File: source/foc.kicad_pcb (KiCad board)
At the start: 2 copper layers, 66.4 x 76.3 mm, 209 parts, among them J1001 Conn_01x04_Male, J1003 TYPE-C-31-M-12, P1 HALL_ENC, P2 SERVO, P3 SWD, P5 PH_A, P6 GND, P7 SUPPLY, P8 PH_B, P9 PH_C, Q1 FMMT593TA, Q10 CSD19536KCS, Q11 CSD19536KCS, Q12 CSD19536KCS, Q13 FMMT593TA, Q14 FMMT593TA, Q15 CSD19536KCS, Q16 CSD19536KCS, Q17 CSD19536KCS, Q18 CSD19536KCS, Q2 FMMT593TA, Q3 NCEP60T20, Q4 CSD19536KCS, Q5 CSD19536KCS, Q6 CSD19536KCS, Q7 FMMT593TA, Q8 FMMT593TA, Q9 CSD19536KCS, U10 TP2604-SR, U1002 TJA1050T/CM,118, U1003 HT7550, U1005 LM1117-3.3, U11 STM32F405RGT6, U2001 BMI160, U4 IRS21867S, U5 IRS21867S, U7 IRS21867S, U8 TX4130L/PW2902, U9 TP2604-SR, Y1001 Crystal_GND24

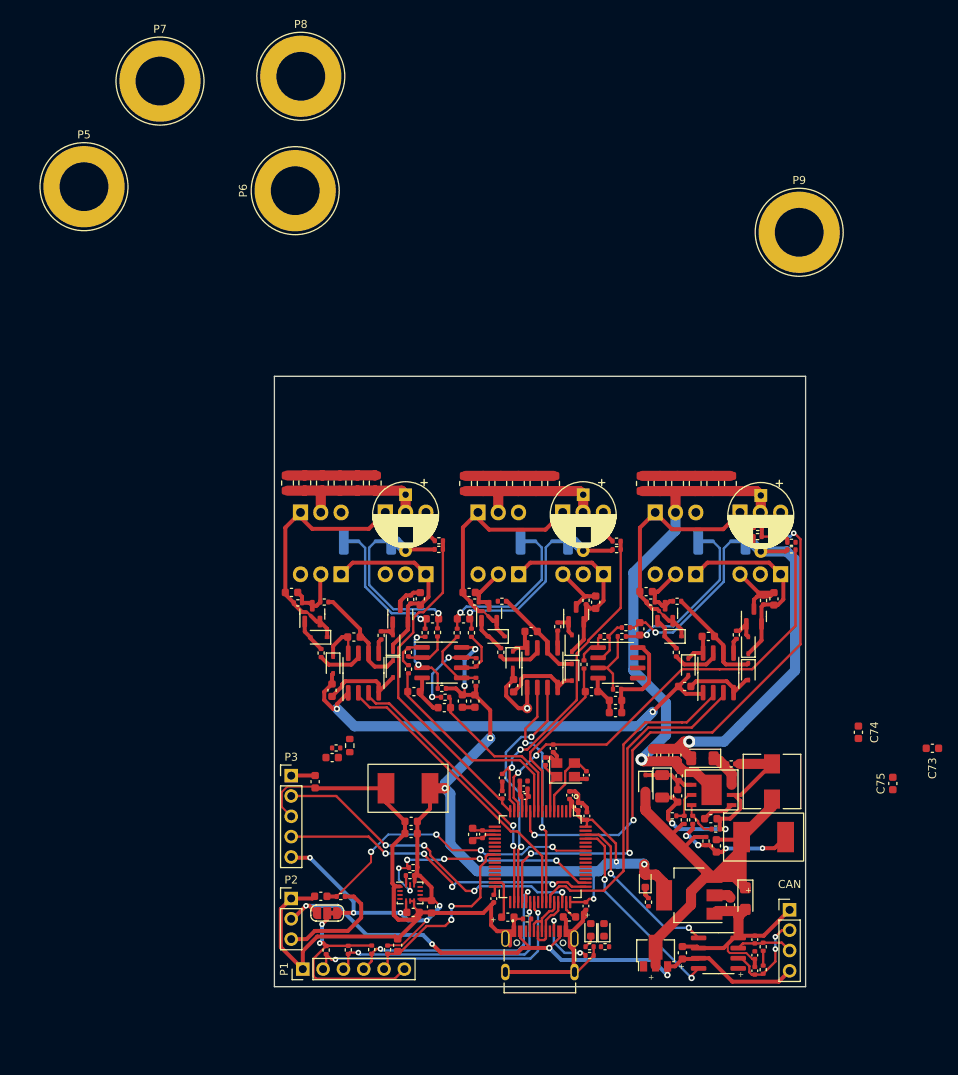
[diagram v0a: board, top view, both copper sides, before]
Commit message: Most components now jlcpcb basic
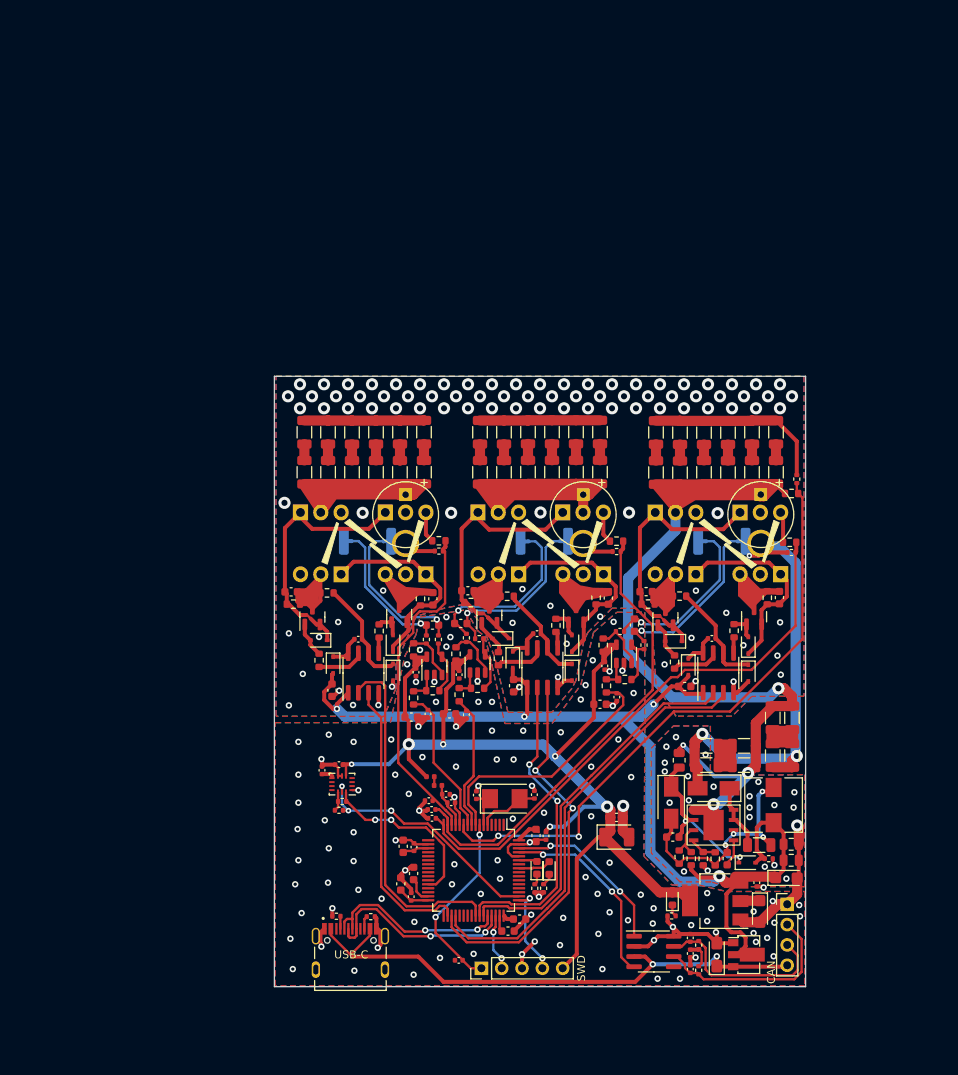
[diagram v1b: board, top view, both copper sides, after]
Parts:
- removed the C1 at (65.6, 139.5)
- removed C1003, C1010: 100n, Capacitor_SMD:C_0402_1005Metric
- removed C1018: 100n, Capacitor_Tantalum_SMD:CP_EIA-3216-18_Kemet-A
- removed the C11 at (76.9, 131.7)
- removed the C2 at (75.2, 145.6)
- removed the C24 at (110.1, 121.8)
- removed the C48 at (85.9, 87.9)
- removed the C49 at (88.1, 87.9)
- removed the C50 at (90.3, 87.9)
- removed the C62 at (112.4, 87.9)
- removed the C63 at (114.6, 87.9)
- removed the C64 at (116.8, 87.9)
- removed the C65 at (120.6, 89.4)
- removed JP1: SolderJumper_3_Bridged12, Jumper:SolderJumper-3_P1.3mm_Bridged12_RoundedPad1.0x1.5mm_NumberLabels
- removed the P1 at (63.4, 148.6)
- removed P2: SERVO, Connector_PinHeader_2.54mm:PinHeader_1x03_P2.54mm_Vertical
- removed P5: PH_A, Connector:Banana_Jack_1Pin
- removed P6: GND, Connector:Banana_Jack_1Pin
- removed P7: SUPPLY, Connector:Banana_Jack_1Pin
- removed P8: PH_B, Connector:Banana_Jack_1Pin
- removed P9: PH_C, Connector:Banana_Jack_1Pin
- removed the R2 at (69.0, 146.2)
- removed the R3 at (66.3, 146.2)
- removed the R4 at (68.1, 139.5)
- removed the R45 at (69.2, 120.7)
- removed the R49 at (67.5, 121.0)
- removed the R8 at (74.0, 146.2)
- removed the U10 at (102.7, 110.3)
- removed the U9 at (80.7, 110.3)
- added C10: 10u@50V, Capacitor_SMD:C_1206_3216Metric, F.Cu at (124.5, 121.9)
- added C103: 100n, Capacitor_SMD:C_0402_1005Metric, F.Cu at (120.1, 137.8)
- added C104: 2.2u, Capacitor_SMD:C_0603_1608Metric, F.Cu at (90.5, 142.3)
- added C105: 2.2u, Capacitor_SMD:C_0603_1608Metric, F.Cu at (92.5, 131.9)
- added C12: 10u@50V, Capacitor_SMD:C_1206_3216Metric, F.Cu at (122.1, 121.9)
- added C14: 10u@50V, Capacitor_SMD:C_1206_3216Metric, F.Cu at (113.8, 120.7)
- added C15: 10u@50V, Capacitor_SMD:C_1206_3216Metric, F.Cu at (118.5, 123.1)
- added C16: 10u@50V, Capacitor_SMD:C_1206_3216Metric, F.Cu at (113.8, 123.1)
- added C22: 22u, Capacitor_SMD:C_0805_2012Metric, F.Cu at (124.4, 135.0)
- added C27: 2.2nF, Capacitor_SMD:C_0603_1608Metric, F.Cu at (61.9, 101.5)
- added C30: 10u @ 50V, Capacitor_SMD:C_1206_3216Metric, F.Cu at (63.5, 86.5)
- added C31: 10u @ 50V, Capacitor_SMD:C_1206_3216Metric, F.Cu at (63.5, 81.5)
- added C33: 10u @ 50V, Capacitor_SMD:C_1206_3216Metric, F.Cu at (66.5, 81.5)
- added C34: 10u @ 50V, Capacitor_SMD:C_1206_3216Metric, F.Cu at (69.5, 86.5)
- added C42: 470u 80V, Custom:CP_Radial_D8.0mm_P5.00mm, F.Cu at (76.2, 89.3)
- added C44: 100n, Capacitor_SMD:C_0402_1005Metric, F.Cu at (82.9, 111.8)
- added C53: 10u @ 50V, Capacitor_SMD:C_1206_3216Metric, F.Cu at (88.5, 81.5)
- added C54: 10u @ 50V, Capacitor_SMD:C_1206_3216Metric, F.Cu at (91.5, 86.5)
- added C55: 10u @ 50V, Capacitor_SMD:C_1206_3216Metric, F.Cu at (91.5, 81.5)
- added C56: 10u @ 50V, Capacitor_SMD:C_1206_3216Metric, F.Cu at (94.5, 86.5)
- added C57: 10u @ 50V, Capacitor_SMD:C_1206_3216Metric, F.Cu at (94.5, 81.5)
- added C61: 10u @ 50V, Capacitor_SMD:C_1206_3216Metric, F.Cu at (100.5, 81.5)
- added C69: 10u @ 50V, Capacitor_SMD:C_1206_3216Metric, F.Cu at (107.5, 86.5)
- added C70: 10u @ 50V, Capacitor_SMD:C_1206_3216Metric, F.Cu at (107.5, 81.5)
- added C71: 10u @ 50V, Capacitor_SMD:C_1206_3216Metric, F.Cu at (110.5, 86.5)
- added C72: 10u @ 50V, Capacitor_SMD:C_1206_3216Metric, F.Cu at (110.5, 81.5)
- added C77: 10u @ 50V, Capacitor_SMD:C_1206_3216Metric, F.Cu at (119.5, 86.5)
- added C78: 10u @ 50V, Capacitor_SMD:C_1206_3216Metric, F.Cu at (119.5, 81.5)
- added C79: 10u @ 50V, Capacitor_SMD:C_1206_3216Metric, F.Cu at (122.5, 86.5)
- added C80: 10u @ 50V, Capacitor_SMD:C_1206_3216Metric, F.Cu at (122.5, 81.5)
- added C81: 470u 80V, Custom:CP_Radial_D8.0mm_P5.00mm, F.Cu at (120.6, 89.3)
- added C9: 10u@50V, Capacitor_SMD:C_1206_3216Metric, F.Cu at (124.5, 117.2)
- added C92: 2.2u, Capacitor_SMD:C_0603_1608Metric, F.Cu at (75.6, 137.9)
- added L2: 15n, Inductor_SMD:L_0402_1005Metric, F.Cu at (80.2, 125.7)
- added NT1: NetTie_2, NetTie:NetTie-2_SMD_Pad0.5mm, B.Cu at (69.0, 95.1)
- added NT2: NetTie_2, NetTie:NetTie-2_SMD_Pad0.5mm, B.Cu at (73.9, 95.1)
- added NT3: NetTie_2, NetTie:NetTie-2_SMD_Pad0.5mm, B.Cu at (91.1, 95.1)
- added NT4: NetTie_2, NetTie:NetTie-2_SMD_Pad0.5mm, B.Cu at (96.0, 95.1)
- added NT5: NetTie_2, NetTie:NetTie-2_SMD_Pad0.5mm, B.Cu at (113.3, 95.1)
- added NT6: NetTie_2, NetTie:NetTie-2_SMD_Pad0.5mm, B.Cu at (118.2, 95.1)
- added U6: MS8311, Custom:SOT-23-5_MS8311, F.Cu at (79.8, 110.7)
- added U7: MS8311, Package_TO_SOT_SMD:TSOT-23-5, F.Cu at (85.2, 110.4)
- added U8: MS8311, Package_TO_SOT_SMD:TSOT-23-5, F.Cu at (103.5, 109.2)
- C1: renamed from C2001; footprint Capacitor_SMD:C_0603_1608Metric -> Capacitor_SMD:C_0402_1005Metric
- C102: renamed from C1008; value 12p -> 15p
- C107: renamed from C1022; footprint Capacitor_SMD:C_0603_1608Metric -> Capacitor_Tantalum_SMD:CP_EIA-3216-10_Kemet-I
- C11: renamed from C21; value 22u @ 100V -> 10u@50V; footprint Capacitor_SMD:C_0603_1608Metric -> Capacitor_SMD:C_1206_3216Metric
- C13: renamed from C23; value 22u @ 100V -> 10u@50V; footprint Capacitor_SMD:C_0603_1608Metric -> Capacitor_SMD:C_1206_3216Metric
- C18: renamed from C25; value 4.7u -> 2.2u
- C19: renamed from C26; footprint Capacitor_SMD:C_0603_1608Metric -> Capacitor_SMD:C_0402_1005Metric
- C2: renamed from C2002; footprint Capacitor_SMD:C_0603_1608Metric -> Capacitor_SMD:C_0402_1005Metric
- C20: renamed from C27; value 4.7u -> 2.2u
- C21: renamed from C28; footprint Capacitor_SMD:C_0603_1608Metric -> Capacitor_SMD:C_0805_2012Metric
- C23: renamed from C29; value C_T491D107K016AT -> 10u; footprint Custom:T491D107K016AT_cap -> Capacitor_Tantalum_SMD:CP_EIA-3216-10_Kemet-I
- C25: renamed from C31; footprint Capacitor_SMD:C_0603_1608Metric -> Capacitor_SMD:C_0402_1005Metric
- C26: renamed from C30; value 1nF -> 1n; footprint Capacitor_SMD:C_0603_1608Metric -> Capacitor_SMD:C_0402_1005Metric
- C29: renamed from C34; value 1n -> 100p
- C32: value 2.2nF -> 10u @ 50V; footprint Capacitor_SMD:C_0603_1608Metric -> Capacitor_SMD:C_1206_3216Metric
- C35, C36, C37, C38, C39, C40, C51, C52, C58, C59, C60: value 4.7u 100V -> 10u @ 50V; footprint Capacitor_SMD:C_0805_2012Metric -> Capacitor_SMD:C_1206_3216Metric
- C41: value 470u 80V -> 10u @ 50V; footprint Capacitor_THT:CP_Radial_D8.0mm_P5.00mm -> Capacitor_SMD:C_1206_3216Metric
- C45: renamed from C42; value 1nF -> 1n; footprint Capacitor_SMD:C_0603_1608Metric -> Capacitor_SMD:C_0402_1005Metric
- C49: renamed from C46; value 1n -> 100p
- C5: renamed from C12; footprint Capacitor_SMD:C_0603_1608Metric -> Capacitor_SMD:C_0402_1005Metric
- C50: renamed from C47; value 4.7u 100V -> 10u @ 50V; footprint Capacitor_SMD:C_0805_2012Metric -> Capacitor_SMD:C_1206_3216Metric
- C6: renamed from C13; value C_T491D107K016AT -> 100u; footprint Custom:T491D107K016AT_cap -> Capacitor_Tantalum_SMD:CP_EIA-3528-21_Kemet-B
- C62: renamed from C53; footprint Capacitor_THT:CP_Radial_D8.0mm_P5.00mm -> Custom:CP_Radial_D8.0mm_P5.00mm
- C63: renamed from C61; footprint Capacitor_SMD:C_0603_1608Metric -> Capacitor_SMD:C_0402_1005Metric
- C65: renamed from C54; value 1nF -> 1n; footprint Capacitor_SMD:C_0603_1608Metric -> Capacitor_SMD:C_0402_1005Metric
- C68: renamed from C57; value 1n -> 100p
- C73, C74, C75, C76: value 2.2u -> 10u @ 50V; footprint Capacitor_SMD:C_0603_1608Metric -> Capacitor_SMD:C_1206_3216Metric
- C8: renamed from C17; footprint Capacitor_SMD:C_0603_1608Metric -> Capacitor_SMD:C_0402_1005Metric
- C88: renamed from C1016; footprint Capacitor_SMD:C_0603_1608Metric -> Capacitor_Tantalum_SMD:CP_EIA-3216-10_Kemet-I_Pad1.58x1.35mm_HandSolder
- C89: renamed from C1011; value 2u2 -> 2.2u
- C90: renamed from C1009; value 2u2 -> 2.2u
- C91: renamed from C1001; value 4u7 -> 2.2u; footprint Capacitor_SMD:C_0402_1005Metric -> Capacitor_SMD:C_0603_1608Metric
- C93: renamed from C71; footprint Capacitor_SMD:C_0603_1608Metric -> Capacitor_SMD:C_0402_1005Metric
- C99: renamed from C1005; value 12p -> 15p
- D6: renamed from D9; value SS510 -> SS210; footprint Diode_SMD:D_1206_3216Metric -> Diode_SMD:D_SMA
- D9: renamed from D12; value SS510 -> SS210; footprint Diode_SMD:D_1206_3216Metric -> Diode_SMD:D_SMA
- L1: renamed from L1001; value 39n -> 15n
- Q1, Q13, Q14, Q2, Q7, Q8: value FMMT593TA -> MMBT5401
- R1: value 2k2 -> R; footprint Resistor_SMD:R_0402_1005Metric -> Custom:field; moved to B.Cu
- R11: renamed from R23; footprint Resistor_SMD:R_0402_1005Metric -> Resistor_SMD:R_0603_1608Metric
- R12: renamed from R24; value 82k -> 82k @ 150V; footprint Resistor_SMD:R_0402_1005Metric -> Resistor_SMD:R_0805_2012Metric
- R13: renamed from R25; value 56k -> 56k @ 75V; footprint Resistor_SMD:R_0402_1005Metric -> Resistor_SMD:R_0603_1608Metric
- R15: renamed from R27; footprint Resistor_SMD:R_0402_1005Metric -> Resistor_SMD:R_0603_1608Metric
- R16: renamed from R28; footprint Resistor_SMD:R_0402_1005Metric -> Resistor_SMD:R_0603_1608Metric
- R17: renamed from R29; footprint Resistor_SMD:R_0402_1005Metric -> Resistor_SMD:R_0603_1608Metric
- R18: renamed from R30; footprint Resistor_SMD:R_0402_1005Metric -> Resistor_SMD:R_0603_1608Metric
- R19: renamed from R31; footprint Resistor_SMD:R_0402_1005Metric -> Resistor_SMD:R_0603_1608Metric
- R20: renamed from R32; value 0.06R -> 0.1R; footprint Resistor_SMD:R_0402_1005Metric -> Resistor_SMD:R_1206_3216Metric
- R21: renamed from R33; value 3k -> 2k
- R22: renamed from R34; footprint Resistor_SMD:R_0402_1005Metric -> Resistor_SMD:R_0603_1608Metric
- R23: renamed from R35; footprint Resistor_SMD:R_0402_1005Metric -> Resistor_SMD:R_0603_1608Metric
- R24: renamed from R36; footprint Resistor_SMD:R_0402_1005Metric -> Resistor_SMD:R_0603_1608Metric
- R25: renamed from R37; footprint Resistor_SMD:R_0402_1005Metric -> Resistor_SMD:R_0603_1608Metric
- R26: renamed from R38; footprint Resistor_SMD:R_0402_1005Metric -> Resistor_SMD:R_0603_1608Metric
- R27: renamed from R39; value 4.7k -> 4.7k @ 75v; footprint Resistor_SMD:R_0402_1005Metric -> Resistor_SMD:R_0603_1608Metric
- R28: renamed from R40; value 4.7k -> 4.7k @ 75v; footprint Resistor_SMD:R_0402_1005Metric -> Resistor_SMD:R_0603_1608Metric
- R32: renamed from R44; footprint Resistor_SMD:R_0402_1005Metric -> Resistor_SMD:R_0603_1608Metric
- R34: renamed from R46; footprint Resistor_SMD:R_0402_1005Metric -> Resistor_SMD:R_0603_1608Metric
- R35: renamed from R47; footprint Resistor_SMD:R_0402_1005Metric -> Resistor_SMD:R_0603_1608Metric
- R36: renamed from R48; footprint Resistor_SMD:R_0402_1005Metric -> Resistor_SMD:R_0603_1608Metric
- R38: renamed from R50; footprint Resistor_SMD:R_0402_1005Metric -> Resistor_SMD:R_0603_1608Metric
- R39: renamed from R51; value 4.7k -> 4.7k @ 75v; footprint Resistor_SMD:R_0402_1005Metric -> Resistor_SMD:R_0603_1608Metric
- R4: renamed from R16; value 56k -> 56k @ 75V; footprint Resistor_SMD:R_0402_1005Metric -> Resistor_SMD:R_0603_1608Metric
- R40: renamed from R52; value 4.7k -> 4.7k @ 75v; footprint Resistor_SMD:R_0402_1005Metric -> Resistor_SMD:R_0603_1608Metric
- R44: renamed from R56; footprint Resistor_SMD:R_0402_1005Metric -> Resistor_SMD:R_0603_1608Metric
- R45: renamed from R57; footprint Resistor_SMD:R_0402_1005Metric -> Resistor_SMD:R_0603_1608Metric
- R46: renamed from R58; footprint Resistor_SMD:R_0402_1005Metric -> Resistor_SMD:R_0603_1608Metric
- R47: renamed from R59; footprint Resistor_SMD:R_0402_1005Metric -> Resistor_SMD:R_0603_1608Metric
- R48: renamed from R60; footprint Resistor_SMD:R_0402_1005Metric -> Resistor_SMD:R_0603_1608Metric
- R49: renamed from R61; value 4.7k -> 4.7k @ 75v; footprint Resistor_SMD:R_0402_1005Metric -> Resistor_SMD:R_0603_1608Metric
- R50: renamed from R62; value 4.7k -> 4.7k @ 75v; footprint Resistor_SMD:R_0402_1005Metric -> Resistor_SMD:R_0603_1608Metric
- R6: renamed from R18; footprint Resistor_SMD:R_0402_1005Metric -> Resistor_SMD:R_0603_1608Metric
- R7: renamed from R19; value 56k -> 56k @ 75V; footprint Resistor_SMD:R_0402_1005Metric -> Resistor_SMD:R_0603_1608Metric
- R9: renamed from R21; value 56k -> 56k @ 75V; footprint Resistor_SMD:R_0402_1005Metric -> Resistor_SMD:R_0603_1608Metric
- U12: renamed from U1005; value LM1117-3.3 -> AMS1117-3.3
- Y1: renamed from Y1001; value Crystal_GND24 -> 8MHz Crystal Resonator, X50328MSB2GI; footprint Crystal:Crystal_SMD_3225-4Pin_3.2x2.5mm -> Crystal:Crystal_SMD_5032-2Pin_5.0x3.2mm
- moved C76 59.5 mm to (116.5, 81.5)
- moved C73 44.8 mm to (113.5, 86.5), turned to -90 degrees
- moved C75 44.0 mm to (116.5, 86.5)
- moved C74 42.1 mm to (113.5, 81.5), turned to -90 degrees
- moved P1 33.8 mm to (85.7, 148.5), turned to 90 degrees
- moved C93 28.6 mm to (82.8, 147.5), turned to 0 degrees
- moved R57 27.8 mm to (71.8, 142.1)
- moved C6 26.8 mm to (102.6, 132.1), turned to 0 degrees
- moved C4 25.7 mm to (102.6, 129.6), turned to 0 degrees
- moved R56 23.8 mm to (67.5, 142.0)
- moved J2 23.7 mm to (69.3, 146.2)
- moved C91 22.4 mm to (75.9, 133.2)
- moved R1 22.2 mm to (91.6, 135.8), turned to 180 degrees
- moved C2 21.9 mm to (65.8, 123.7), turned to -90 degrees
- moved C1 20.7 mm to (67.9, 123.0), turned to 0 degrees
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- renumbered C1012 to C101, C22 to C17, C2003 to C24, C33 to C28, C8 to C3, C10 to C4, C44 to C47, C45 to C48, C2004 to C64, C55 to C66, C56 to C67, C14 to C7, C1013 to C82, C1021 to C83, C1020 to C84, C1019 to C85, C1014 to C86, C1015 to C87, C1002 to C94, C1004 to C96, C1006 to C97, C1007 to C98, D4 to D1, D13 to D10, D14 to D11, D17 to D12, D18 to D13, D21 to D14, D22 to D15, D1001 to D16, D1002 to D17, D1003 to D18, D5 to D2, D6 to D3, D7 to D4, D8 to D5, D10 to D7, D11 to D8, J1001 to J1, J1003 to J2, P3 to P1, R22 to R10, R26 to R14, R2001 to R2, R41 to R29, R2002 to R3, R42 to R30, R43 to R31, R53 to R41, R54 to R42, R55 to R43, R17 to R5, R63 to R51, R64 to R52, R65 to R53, R1006 to R54, R1007 to R55, R1010 to R56, R1011 to R57, R1001 to R58, R1002 to R59, R1003 to R60, R20 to R8, U2001 to U1, U1003 to U10, U4 to U2, U5 to U3, U7 to U4, U8 to U5, U1002 to U9
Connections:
- C11 pad 2: GND -> Net-(C11-Pad2)
- C13 pad 2: GND -> Net-(C13-Pad2)
- C28 pad 2: Net-(C33-Pad2) -> Net-(C28-Pad2)
- C29 pad 1: GND -> Net-(C29-Pad1)
- C29 pad 2: Net-(C33-Pad2) -> Net-(C29-Pad2)
- C32 pad 2: /driver/HS1 -> V_IN
- C35 pad 2: V_IN -> Net-(C34-Pad1)
- C36 pad 1: GND -> Net-(C36-Pad1)
- C37 pad 2: V_IN -> Net-(C36-Pad1)
- C38 pad 1: GND -> Net-(C38-Pad1)
- C39 pad 2: V_IN -> Net-(C38-Pad1)
- C40 pad 1: GND -> Net-(C40-Pad1)
- C41 pad 1: V_IN -> GND
- C41 pad 2: GND -> Net-(C40-Pad1)
- C43 pad 2: /mcu/ADC_TEMP -> VCC
- C48 pad 2: Net-(C45-Pad2) -> Net-(C48-Pad2)
- C49 pad 1: GND -> Net-(C49-Pad1)
- C49 pad 2: Net-(C45-Pad2) -> Net-(C49-Pad2)
- C50 pad 1: GND -> Net-(C50-Pad1)
- C51 pad 2: V_IN -> Net-(C50-Pad1)
- C52 pad 1: GND -> Net-(C52-Pad1)
- C58 pad 1: GND -> Net-(C58-Pad1)
- C59 pad 2: V_IN -> Net-(C58-Pad1)
- C60 pad 1: GND -> Net-(C60-Pad1)
- C63 pad 1: GND -> VCC
- C63 pad 2: VCC -> GND
- C64 pad 1: GND -> VCC
- C64 pad 2: VCC -> GND
- C67 pad 2: Net-(C56-Pad2) -> Net-(C67-Pad2)
- C68 pad 1: GND -> Net-(C68-Pad1)
- C68 pad 2: Net-(C56-Pad2) -> Net-(C68-Pad2)
- C73 pad 1: GND -> Net-(C73-Pad1)
- C73 pad 2: VCC -> V_IN
- C74 pad 2: VCC -> Net-(C73-Pad1)
- C75 pad 1: GND -> Net-(C75-Pad1)
- C75 pad 2: VCC -> V_IN
- C76 pad 2: VCC -> Net-(C75-Pad1)
- D10 pad 1: Net-(C32-Pad1) -> Net-(C27-Pad1)
- L1 pad 2: /mcu/3.3VA -> Net-(L1-Pad2)
- Q1 pad 2: Net-(C32-Pad1) -> Net-(C27-Pad1)
- Q10 pad 3: Net-(C45-Pad2) -> Net-(C48-Pad2)
- Q12 pad 3: Net-(C45-Pad2) -> Net-(C48-Pad2)
- Q14 pad 3: Net-(C56-Pad2) -> Net-(C67-Pad2)
- Q16 pad 3: Net-(C56-Pad2) -> Net-(C67-Pad2)
- Q18 pad 3: Net-(C56-Pad2) -> Net-(C67-Pad2)
- Q2 pad 3: Net-(C33-Pad2) -> Net-(C28-Pad2)
- Q3 pad 1: Net-(C32-Pad1) -> Net-(C27-Pad1)
- Q4 pad 3: Net-(C33-Pad2) -> Net-(C28-Pad2)
- Q5 pad 1: Net-(C32-Pad1) -> Net-(C27-Pad1)
- Q6 pad 3: Net-(C33-Pad2) -> Net-(C28-Pad2)
- Q8 pad 3: Net-(C45-Pad2) -> Net-(C48-Pad2)
- R27 pad 2: Net-(C32-Pad1) -> Net-(C27-Pad1)
- R28 pad 1: Net-(C33-Pad2) -> Net-(C28-Pad2)
- R29 pad 1: Net-(C33-Pad2) -> Net-(C29-Pad2)
- R30 pad 1: GND -> Net-(C29-Pad1)
- R31 pad 1: Net-(C33-Pad2) -> Net-(C28-Pad2)
- R40 pad 1: Net-(C45-Pad2) -> Net-(C48-Pad2)
- R41 pad 1: Net-(C45-Pad2) -> Net-(C49-Pad2)
- R42 pad 1: GND -> Net-(C49-Pad1)
- R43 pad 1: Net-(C45-Pad2) -> Net-(C48-Pad2)
- R50 pad 1: Net-(C56-Pad2) -> Net-(C67-Pad2)
- R51 pad 1: Net-(C56-Pad2) -> Net-(C68-Pad2)
- R52 pad 1: GND -> Net-(C68-Pad1)
- R53 pad 1: Net-(C56-Pad2) -> Net-(C67-Pad2)
- U11 pad 14: /driver/SENS_3 -> /driver/SENS_1
- U11 pad 16: /driver/SENS_1 -> /driver/SENS_3
- Y1 pad 2: GND -> /mcu/PH1
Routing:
- net GND: track 401.4 -> 254.0 mm, vias 8 -> 237
- net /mcu/SERVO: track 37.9 -> 0.00 mm, vias 4 -> 0
- net /mcu/HALL_3: track 36.2 -> 0.00 mm, vias 2 -> 0
- net Net-(C27-Pad1): track 0.00 -> 34.0 mm
- net /mcu/SWDIO: track 40.9 -> 7.12 mm, vias 4 -> 2
- net Net-(C32-Pad1): track 35.3 -> 2.04 mm
- net /mcu/HALL_2: track 31.4 -> 0.00 mm, vias 2 -> 0
- net Net-(C56-Pad2): track 31.1 -> 0.00 mm, vias 1 -> 0
- net /mcu/HALL_1: track 30.4 -> 0.00 mm, vias 2 -> 0
- net Net-(C45-Pad2): track 29.4 -> 0.00 mm, vias 1 -> 0
- net /mcu/SWCLK: track 40.5 -> 11.3 mm, vias 4 -> 2
- net Net-(JP1-Pad2): track 27.2 -> 0.00 mm, vias 2 -> 0
- net V_IN: track 118.3 -> 144.7 mm, vias 1 -> 4
- net /mcu/TEMP_MOTOR: track 24.2 -> 0.00 mm, vias 2 -> 0
- net Net-(C49-Pad2): track 0.00 -> 22.0 mm, vias 0 -> 1
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- added copper zone on B.Cu, net GND
- added copper zone on F.Cu, net GND
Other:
- board text added: "USB-C"
- board text removed: "+"

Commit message: Add files via upload
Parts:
- removed C13, C14, C15, C16: 10u@50V, Capacitor_SMD:C_1206_3216Metric
- removed the C43 at (81.7, 116.7)
- removed the C44 at (82.9, 111.8)
- removed the C45 at (83.8, 116.8)
- removed the C49 at (83.1, 105.4)
- removed L2: 15n, Inductor_SMD:L_0402_1005Metric
- removed the R11 at (88.9, 102.0)
- removed the R14 at (124.4, 96.5)
- removed the R16 at (110.5, 102.0)
- removed the R35 at (95.0, 105.6)
- removed the R40 at (100.0, 102.2)
- removed the R41 at (83.8, 107.2)
- removed the R53 at (115.7, 95.1)
- removed the U7 at (85.2, 110.4)
- added C100: 100n, Capacitor_SMD:C_0603_1608Metric, F.Cu at (29.8, 94.0)
- added C106: 2.2u, Capacitor_SMD:C_0603_1608Metric, F.Cu at (89.7, 128.8)
- added C108: 2.2u, Capacitor_SMD:C_0603_1608Metric, F.Cu at (33.8, 91.5)
- added C24: 2.2u, Capacitor_SMD:C_0603_1608Metric, F.Cu at (73.7, 108.8)
- added C25: 100n, Capacitor_SMD:C_0603_1608Metric, F.Cu at (75.3, 108.8)
- added C26: 1n, Capacitor_SMD:C_0603_1608Metric, F.Cu at (79.0, 129.4)
- added C29: 100p, Capacitor_SMD:C_0603_1608Metric, F.Cu at (79.4, 102.4)
- added C46: 2.2u, Capacitor_SMD:C_0603_1608Metric, F.Cu at (42.9, 91.5)
- added C95: 100n, Capacitor_SMD:C_0603_1608Metric, F.Cu at (33.8, 94.0)
- added R12: 56k @ 75V, Resistor_SMD:R_0603_1608Metric, F.Cu at (125.5, 89.7)
- added R15: 2R, Resistor_SMD:R_0603_1608Metric, F.Cu at (110.8, 104.8)
- added R21: 30k, Resistor_SMD:R_0603_1608Metric, F.Cu at (75.9, 112.0)
- added R24: 30k, Resistor_SMD:R_0603_1608Metric, F.Cu at (78.2, 111.2)
- added R25: 62k, Resistor_SMD:R_0603_1608Metric, F.Cu at (75.8, 105.4)
- added R28: 1k, Resistor_SMD:R_0603_1608Metric, F.Cu at (78.1, 104.7)
- added R29: 1k, Resistor_SMD:R_0603_1608Metric, F.Cu at (79.6, 104.7)
- added R33: 4.7R, Resistor_SMD:R_0603_1608Metric, F.Cu at (83.4, 111.2)
- added R8: 56k @ 75V, Resistor_SMD:R_0603_1608Metric, F.Cu at (103.2, 89.7)
- added U6: MS8311, Custom:SOT-23-5_MS8311, F.Cu at (77.8, 108.3)
- C1, C101, C102, C103, C19, C2, C5, C63, C65, C8, C82, C83, C84, C85, C86, C87, C93, C94, C96, C97, C98, C99: footprint Capacitor_SMD:C_0402_1005Metric -> Capacitor_SMD:C_0603_1608Metric
- C44: renamed from C25; footprint Capacitor_SMD:C_0402_1005Metric -> Capacitor_SMD:C_0603_1608Metric
- C45: renamed from C26; footprint Capacitor_SMD:C_0402_1005Metric -> Capacitor_SMD:C_0603_1608Metric
- L1: value 15n -> 30n; footprint Inductor_SMD:L_0402_1005Metric -> Inductor_SMD:L_0603_1608Metric
- R1: renamed from R2; footprint Resistor_SMD:R_0402_1005Metric -> Resistor_SMD:R_0603_1608Metric
- R10: value 2k -> 2R; footprint Resistor_SMD:R_0402_1005Metric -> Resistor_SMD:R_0603_1608Metric
- R13, R9: value 56k @ 75V -> 2k
- R2: renamed from R3; footprint Resistor_SMD:R_0402_1005Metric -> Resistor_SMD:R_0603_1608Metric
- R20: renamed from R21; footprint Resistor_SMD:R_0402_1005Metric -> Resistor_SMD:R_0603_1608Metric
- R32: value 30k -> NTC 10k; footprint Resistor_SMD:R_0603_1608Metric -> Resistor_SMD:R_0402_1005Metric
- R36: value 30k -> 10k; footprint Resistor_SMD:R_0603_1608Metric -> Resistor_SMD:R_0402_1005Metric
- R38, R48: value 62k -> 4.7k @ 75v
- R4: renamed from R5; footprint Resistor_SMD:R_0402_1005Metric -> Resistor_SMD:R_0603_1608Metric
- R40: renamed from R29; footprint Resistor_SMD:R_0402_1005Metric -> Resistor_SMD:R_0603_1608Metric
- R41: renamed from R30; footprint Resistor_SMD:R_0402_1005Metric -> Resistor_SMD:R_0603_1608Metric
- R42, R52: value 1k -> ASR-M-3-0.25F 0.25mR; footprint Resistor_SMD:R_0402_1005Metric -> Resistor_SMD:R_2512_6332Metric; moved to B.Cu
- R43: value ASR-M-3-0.25F 0.25mR -> 30k; footprint Resistor_SMD:R_2512_6332Metric -> Resistor_SMD:R_0603_1608Metric; moved to F.Cu
- R44: value 30k -> 4.7R
- R46: value 4.7R -> 30k
- R47: value 30k -> 62k
- R50: value 4.7k @ 75v -> 1k
- R51: footprint Resistor_SMD:R_0402_1005Metric -> Resistor_SMD:R_0603_1608Metric
- R53: renamed from R54; footprint Resistor_SMD:R_0402_1005Metric -> Resistor_SMD:R_0603_1608Metric
- R54: renamed from R55; footprint Resistor_SMD:R_0402_1005Metric -> Resistor_SMD:R_0603_1608Metric
- R55: renamed from R56; footprint Resistor_SMD:R_0402_1005Metric -> Resistor_SMD:R_0603_1608Metric
- R56: renamed from R57; footprint Resistor_SMD:R_0402_1005Metric -> Resistor_SMD:R_0603_1608Metric
- R57: renamed from R58; footprint Resistor_SMD:R_0402_1005Metric -> Resistor_SMD:R_0603_1608Metric
- R58: renamed from R59; footprint Resistor_SMD:R_0402_1005Metric -> Resistor_SMD:R_0603_1608Metric
- R59: renamed from R60; footprint Resistor_SMD:R_0402_1005Metric -> Resistor_SMD:R_0603_1608Metric
- R7: renamed from R8; footprint Resistor_SMD:R_0402_1005Metric -> Resistor_SMD:R_0603_1608Metric
- U7: renamed from U6; footprint Custom:SOT-23-5_MS8311 -> Package_TO_SOT_SMD:TSOT-23-5
- moved R36 44.8 mm to (46.4, 91.2), turned to 0 degrees
- moved R7 43.3 mm to (82.0, 82.9)
- moved R6 42.6 mm to (82.0, 85.9), turned to -90 degrees
- moved R32 42.2 mm to (46.4, 93.2), turned to 0 degrees
- moved C98 33.0 mm to (49.5, 121.6)
- moved C96 32.4 mm to (49.5, 120.1)
- moved R43 31.7 mm to (120.5, 111.8), turned to -90 degrees
- moved L1 31.6 mm to (48.3, 118.6)
- moved C49 22.5 mm to (101.8, 102.3)
- moved R41 22.0 mm to (102.1, 104.6)
- moved R40 22.0 mm to (100.6, 104.6)
- moved R37 21.4 mm to (98.3, 105.3), turned to 180 degrees
- moved R51 21.4 mm to (124.3, 104.6), turned to -90 degrees
- moved R31 21.4 mm to (98.3, 111.8)
- moved R35 21.2 mm to (100.7, 111.1)
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- renumbered C24 to C43, C29 to C49, R1 to FieldFeets1, R12 to R11, R15 to R14, R17 to R16, R18 to R17, R19 to R18, R20 to R19, R23 to R22, R24 to R23, R27 to R26, R28 to R27, R4 to R3, R31 to R30, R22 to R31, R25 to R35, R26 to R37, R6 to R5, R7 to R6
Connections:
- C45 pad 2: /mcu/CURRENT_1 -> /mcu/CURRENT_2
- C49 pad 1: Net-(C29-Pad1) -> Net-(C49-Pad1)
- C49 pad 2: Net-(C29-Pad2) -> Net-(C49-Pad2)
- L1 pad 2: Net-(L1-Pad2) -> /mcu/3.3VA
- R10 pad 1: /driver/SENS_2 -> Net-(C8-Pad2)
- R10 pad 2: GND -> /driver/HS2
- R13 pad 2: /driver/HS3 -> GND
- R31 pad 2: /mcu/CURRENT_1 -> /mcu/CURRENT_2
- R32 pad 1: Net-(R32-Pad1) -> /mcu/ADC_TEMP
- R32 pad 2: /mcu/CURRENT_2 -> VCC
- R34 pad 1: /driver/HO2 -> /driver/LO2
- R34 pad 2: Net-(D12-Pad2) -> Net-(D13-Pad2)
- R36 pad 1: Net-(R36-Pad1) -> GND
- R36 pad 2: Net-(R32-Pad1) -> /mcu/ADC_TEMP
- R38 pad 1: Net-(R38-Pad1) -> /driver/HS2
- R38 pad 2: VCC -> Net-(C47-Pad1)
- R39 pad 1: /driver/HS2 -> Net-(C48-Pad2)
- R39 pad 2: Net-(C47-Pad1) -> Net-(C48-Pad1)
- R40 pad 1: Net-(C29-Pad2) -> Net-(C49-Pad2)
- R41 pad 1: Net-(C29-Pad1) -> Net-(C49-Pad1)
- R42 pad 1: Net-(C49-Pad1) -> Net-(C48-Pad2)
- R42 pad 2: Net-(R36-Pad1) -> GND
- R43 pad 1: Net-(C48-Pad2) -> Net-(R43-Pad1)
- R43 pad 2: GND -> /mcu/CURRENT_3
- R44 pad 1: Net-(R44-Pad1) -> /driver/HO3
- R44 pad 2: /mcu/CURRENT_3 -> Net-(D14-Pad2)
- R45 pad 1: /driver/HO3 -> /driver/LO3
- R45 pad 2: Net-(D14-Pad2) -> Net-(D15-Pad2)
- R46 pad 1: /driver/LO3 -> Net-(R46-Pad1)
- R46 pad 2: Net-(D15-Pad2) -> Net-(R43-Pad1)
- R47 pad 2: Net-(R44-Pad1) -> VCC
- R48 pad 1: Net-(R48-Pad1) -> /driver/HS3
- R48 pad 2: VCC -> Net-(C66-Pad1)
- R49 pad 1: /driver/HS3 -> Net-(C67-Pad2)
- R49 pad 2: Net-(C66-Pad1) -> Net-(C67-Pad1)
- R50 pad 1: Net-(C67-Pad2) -> Net-(C68-Pad2)
- R50 pad 2: Net-(C67-Pad1) -> Net-(R47-Pad1)
- R51 pad 1: Net-(C68-Pad2) -> Net-(C68-Pad1)
- R51 pad 2: Net-(R48-Pad1) -> Net-(R46-Pad1)
- R52 pad 1: Net-(C68-Pad1) -> Net-(C67-Pad2)
- R52 pad 2: Net-(R47-Pad1) -> GND
- R9 pad 2: /driver/HS2 -> GND
- U11 pad 10: /mcu/CURRENT_1 -> /driver/SENS_2
- U11 pad 11: /driver/SENS_SUPPLY -> /mcu/CURRENT_2
- U11 pad 14: /driver/SENS_1 -> /driver/SENS_SUPPLY
- U11 pad 15: /driver/SENS_2 -> /driver/SENS_1
- U11 pad 16: /driver/SENS_3 -> /mcu/CURRENT_1
- U11 pad 9: /mcu/CURRENT_2 -> /driver/SENS_3
- U8 pad 1: Net-(R44-Pad1) -> Net-(R43-Pad1)
- U8 pad 3: Net-(R48-Pad1) -> Net-(R47-Pad1)
- U8 pad 4: Net-(R47-Pad1) -> Net-(R46-Pad1)
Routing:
- net +12V: track 135.3 -> 197.3 mm, vias 4 -> 6
- net GND: track 254.0 -> 206.4 mm, vias 237 -> 160
- net VCC: track 161.9 -> 199.3 mm, vias 6 -> 4
- net /driver/SENS_SUPPLY: track 76.2 -> 50.1 mm, vias 2 -> 0
- net /driver/HS2: track 3.93 -> 19.0 mm
- net V_IN: track 144.7 -> 129.7 mm, vias 4 -> 0
- net /mcu/CURRENT_3: track 32.0 -> 46.0 mm
- net +5V: track 70.0 -> 58.5 mm
- net Net-(C48-Pad2): track 15.3 -> 3.90 mm
- net /mcu/CURRENT_2: track 17.0 -> 28.2 mm
- net Net-(C67-Pad2): track 14.1 -> 4.18 mm
- net /driver/H2: track 39.0 -> 47.3 mm, vias 2 -> 6
- net Net-(R36-Pad1): track 6.89 -> 0.00 mm
- net /driver/HS1: track 12.2 -> 19.0 mm
- net Net-(R48-Pad1): track 6.70 -> 0.00 mm
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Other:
- board size 66.4 x 76.3 mm -> 68 x 79 mm
- board text added: "NORDSTREAM3"
- board text added: "github.com/nordstream3/"
